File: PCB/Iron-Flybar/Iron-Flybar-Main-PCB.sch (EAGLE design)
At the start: 49 parts, among them IC1 STM32F10XCXT6, U1 MA01-3W, U2 MA01-3W, U3 MA01-3W, U4 MA01-3W, U5 MA01-3W, U6 MA01-3W, U7 3B-ZR, U8 3B-ZR, X1 MINI-USB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

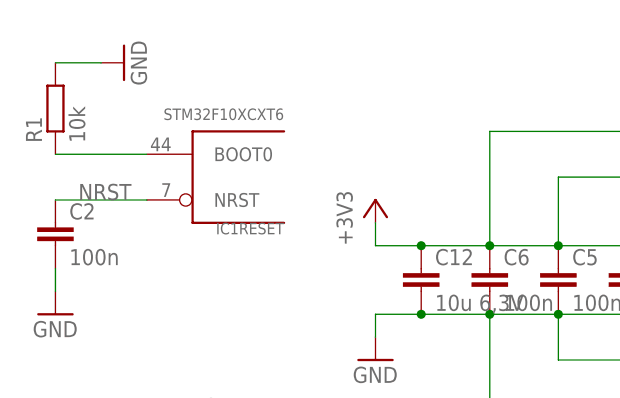
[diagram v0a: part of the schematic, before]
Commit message: Datasheets and PCB added
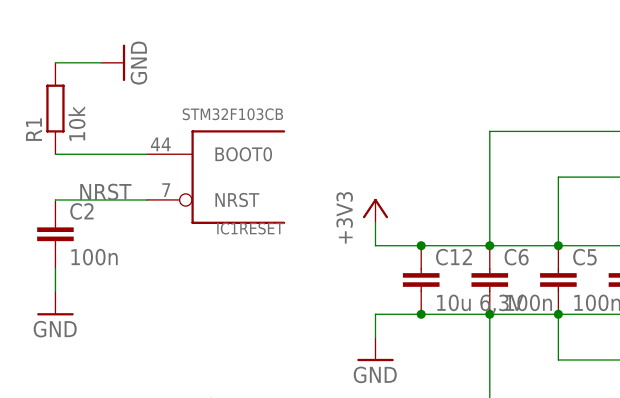
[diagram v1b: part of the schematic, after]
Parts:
- IC1: value STM32F10XCXT6 -> STM32F103CB
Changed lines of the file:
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@@
 <?xml version="1.0" encoding="utf-8"?>
 <!DOCTYPE eagle SYSTEM "eagle.dtd">
-<eagle version="6.3">
+<eagle version="6.4">
 <drawing>
 <settings>
@@
 <part name="+3V2" library="supply1" deviceset="+3V3" device=""/>
 <part name="GND6" library="supply1" deviceset="GND" device=""/>
-<part name="IC1" library="stm32" deviceset="STM32F10XCXT6" device=""/>
+<part name="IC1" library="stm32" deviceset="STM32F10XCXT6" device="" value="STM32F103CB"/>
 <part name="R1" library="rcl" deviceset="R-EU_" device="R0603" value="10k"/>
 <part name="U$2" library="linear-technology-2" deviceset="LT1761" device=""/>
